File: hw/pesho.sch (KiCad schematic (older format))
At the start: 25 parts

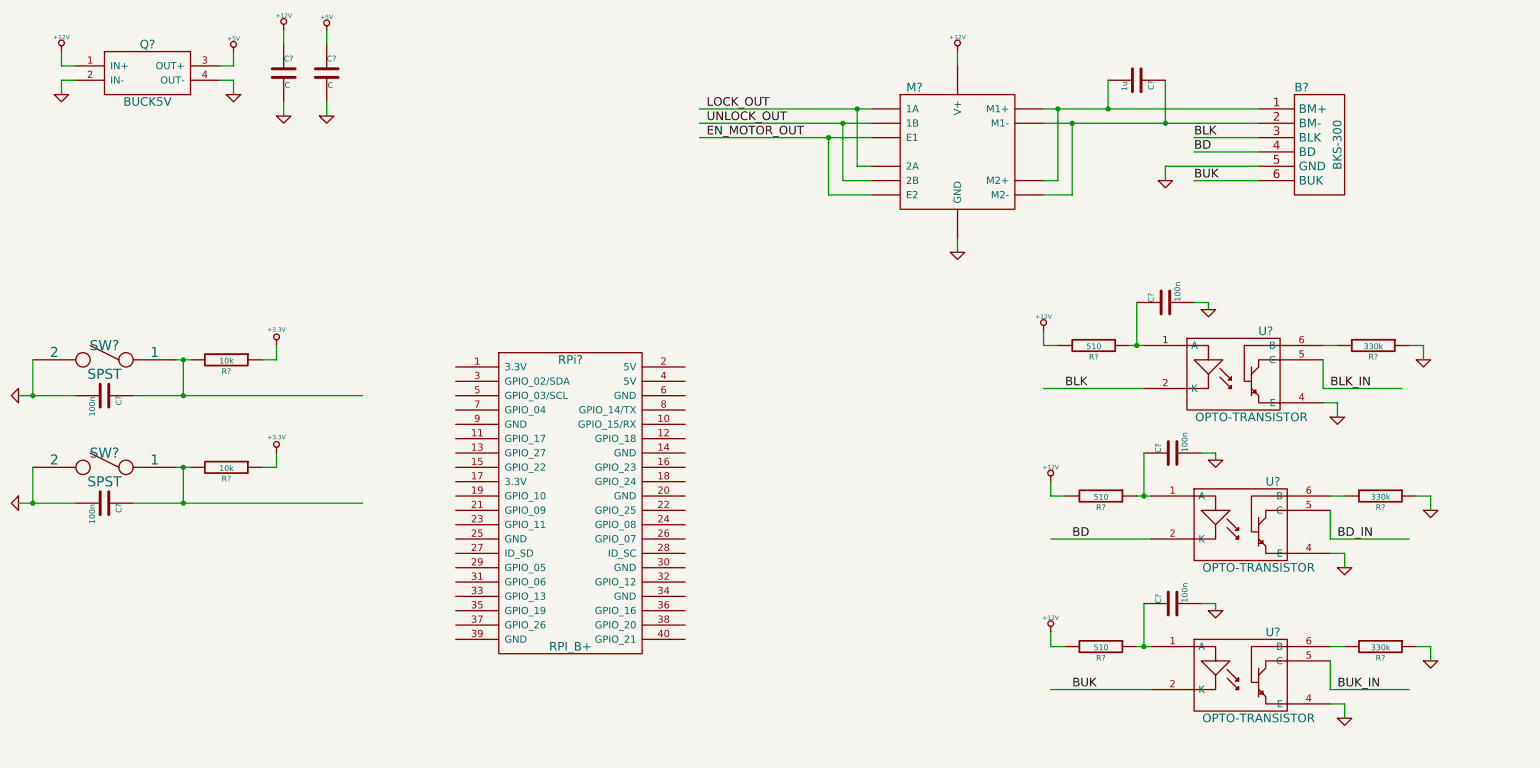
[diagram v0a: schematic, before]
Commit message: changed values of the resistors and added connections to the rpi
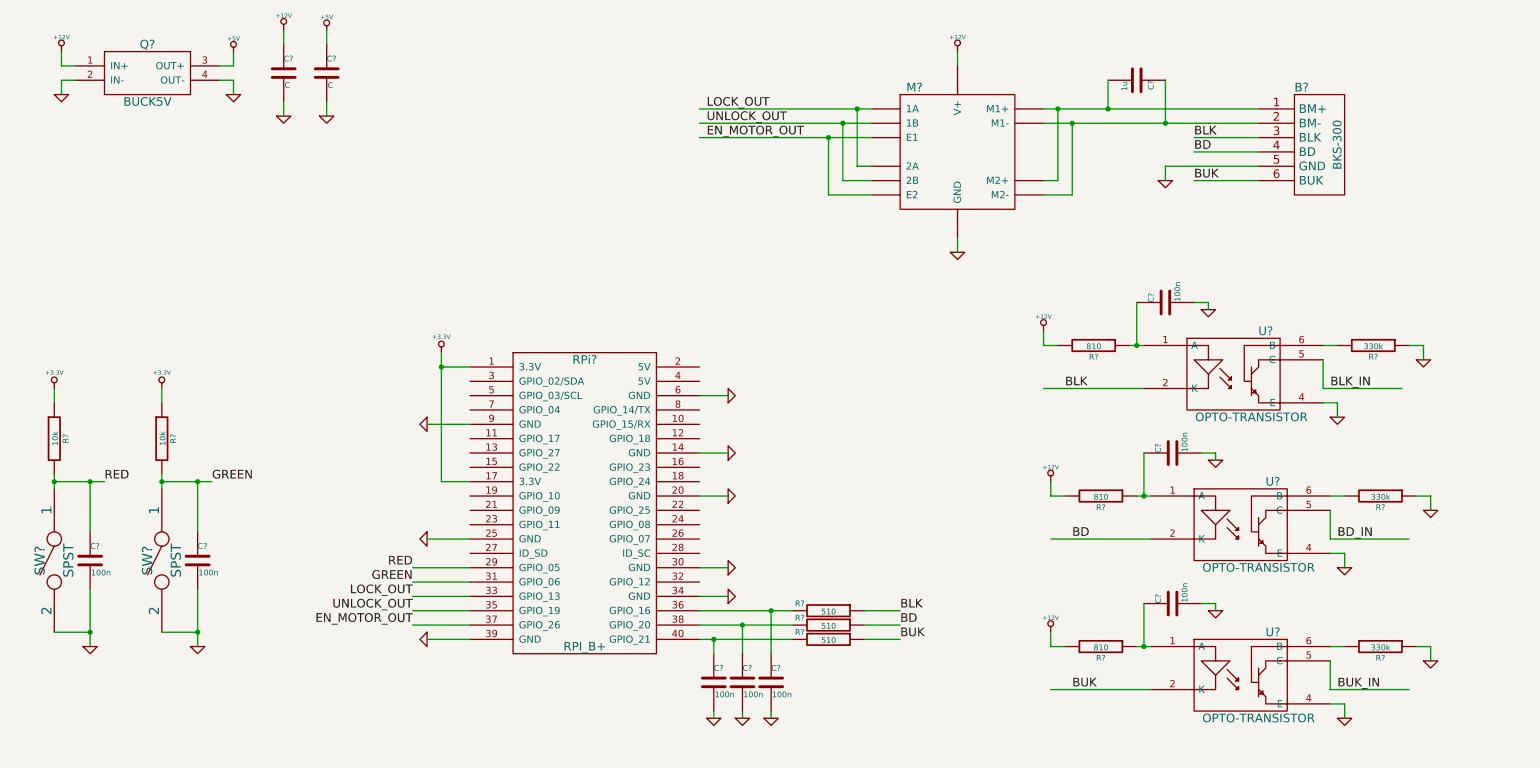
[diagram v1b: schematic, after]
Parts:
- added C? (x3): 100n, symbol C
- added R? (x3): 510, symbol R
- R? (x3): value 510 -> 810
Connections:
- net labels added: GREEN, RED
- wire segments 92 -> 138
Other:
- moved on the sheet: C?, R?, RPi?, SW?

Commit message: some explanations
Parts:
- removed C? (x2): 100n, symbol C
- removed C?: 1u, symbol C
- removed C? (x2): C, symbol C
- removed R? (x2): 330k, symbol R
- removed R? (x2): 810, symbol R
- removed U? (x2): OPTO-TRANSISTOR, symbol OPTO-TRANSISTOR
- added C?: 220u, symbol CAPAPOL
- added C? (x3): C, symbol C
- added C? (x2): 100n, symbol C
- added R? (x2): 330k, symbol R
- added R? (x2): 810, symbol R
- added U? (x2): OPTO-TRANSISTOR, symbol OPTO-TRANSISTOR
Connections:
- wire segments 138 -> 117
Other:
- note added: "40-pin конектор към\nRaspberry Pi B+"
- note added: "Бутони на панела\nна кутията"
- note added: "Двоен драйвер за мотор"
- note added: "Импулсен step-down модул"
- note added: "Клеморед към\nбравата"
- moved on the sheet: C?, Q?, R?
